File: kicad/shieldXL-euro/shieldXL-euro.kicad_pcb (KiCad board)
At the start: 2 copper layers, 98 x 108 mm, 134 parts, among them J101 Eurorack power, J102 IN L, J103 IN R, J104 OUT L, J105 OUT R, J106 MIDI IN, J107 MIDI OUT, J108 DX07S024WJ1R350, J109 USB 1, J110 USB 2, J111 USB 3, J112 Pi USB, inner stack, J113 Pi USB, outer stack, J115 CORONE I/1, J116 CORONE I/2, J117 CORONE O/1, J118 CORONE O/2, J119 CORONE O/3, J120 CORONE O/4, J121 Corone, J122 ii, Q1 ASFL1-12.288MHZ-LCS-T, SW1 D6R00 F1 LFS, SW2 D6R00 F1 LFS, SW3 D6R00 F1 LFS, U1 CS4270, U101 TL074, U11 TPS793475DBVR, U2 HCPL-0631-500E, X1 RASPI_BOARD_B+#_E3

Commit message: Board: MIDI LEDs on their panel holes, locked
D1 / D2 (red 3 mm) at panel (50.35, 96.5) / (50.35, 102.5) between the MIDI
jacks; F8 had left shieldXL's 0603 LEDs beside them under the same
references, removed. Panel layer redrawn with the LED holes and marks.

Co-Authored-By: Claude Opus 5.5 <noreply@anthropic.com>
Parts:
- added C114: 47u 10V, Capacitor_SMD:C_1206_3216Metric, F.Cu at (85.2, 167.3)
- added C115: 47u 10V, Capacitor_SMD:C_1206_3216Metric, F.Cu at (85.2, 170.6)
- added C116: 47u 10V, Capacitor_SMD:C_1206_3216Metric, F.Cu at (85.2, 174.0)
- added C117: 100n, Capacitor_SMD:C_0805_2012Metric, F.Cu at (80.2, 167.1)
- added C118: 100n, Capacitor_SMD:C_0805_2012Metric, F.Cu at (80.2, 170.1)
- added C119: 100n, Capacitor_SMD:C_0805_2012Metric, F.Cu at (80.2, 173.1)
- added C120: 100n, Capacitor_SMD:C_0805_2012Metric, F.Cu at (80.2, 176.1)
- added C121: 10u, Capacitor_SMD:C_0805_2012Metric, F.Cu at (80.2, 179.1)
- added C122: 100n, Capacitor_SMD:C_0805_2012Metric, F.Cu at (80.2, 182.1)
- added JP103: AGND-GND, Jumper:SolderJumper-2_P1.3mm_Open_Pad1.0x1.5mm, F.Cu at (84.6, 177.4)
- added U102: USBLC6-2SC6, Package_TO_SOT_SMD:SOT-23-6, F.Cu at (75.4, 168.0)
- added U103: USBLC6-2SC6, Package_TO_SOT_SMD:SOT-23-6, F.Cu at (75.4, 172.6)
- added U104: USBLC6-2SC6, Package_TO_SOT_SMD:SOT-23-6, F.Cu at (75.4, 177.2)
- added U105: 74LVC1G125, Package_TO_SOT_SMD:SOT-23-5, F.Cu at (75.4, 181.9)
- D1: value RED -> RED 3mm; footprint ShieldXL:CHIPLED_0603_NOOUTLINE -> MMM:LED_3mm_PadsAC; moved to F.Cu
- D2: value BLUE -> RED 3mm; footprint ShieldXL:CHIPLED_0603_NOOUTLINE -> MMM:LED_3mm_PadsAC; moved to F.Cu
- R101, R103: value 100k -> 69.8k
- R102, R104: value 40.2k -> 30.1k
- R17: value 47Ω -> 100Ω
- R19: value 47Ω -> 470Ω
- R20: value 15Ω -> 470Ω
- moved D2 72.9 mm to (150.3, 132.5)
- moved D1 65.7 mm to (150.3, 126.5)
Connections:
- C105 pad 1: /eurorack/INL_SUM -> /eurorack/INL_DIV
- C105 pad 2: IN_L_LINE -> AGND
- C106 pad 1: /eurorack/INR_SUM -> /eurorack/INR_DIV
- C106 pad 2: IN_R_LINE -> AGND
- D2 pad C: MIDI_TX -> MIDI_TX_BUF
- R101 pad 2: /eurorack/INL_SUM -> /eurorack/INL_DIV
- R102 pad 1: /eurorack/INL_SUM -> /eurorack/INL_DIV
- R102 pad 2: IN_L_LINE -> AGND
- R103 pad 2: /eurorack/INR_SUM -> /eurorack/INR_DIV
- R104 pad 1: /eurorack/INR_SUM -> /eurorack/INR_DIV
- R104 pad 2: IN_R_LINE -> AGND
- R17 pad 2: MIDI_TX -> MIDI_TX_BUF
- U101 pad 2: /eurorack/INL_SUM -> IN_L_LINE
- U101 pad 3: AGND -> /eurorack/INL_DIV
- U101 pad 5: AGND -> /eurorack/INR_DIV
- U101 pad 6: /eurorack/INR_SUM -> IN_R_LINE
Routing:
- net IN_R_LINE: track 15.8 -> 35.9 mm
- net /eurorack/INR_SUM: track 20.0 -> 0.00 mm
- net IN_L_LINE: track 6.16 -> 18.2 mm
- net /eurorack/INL_SUM: track 12.1 -> 0.00 mm

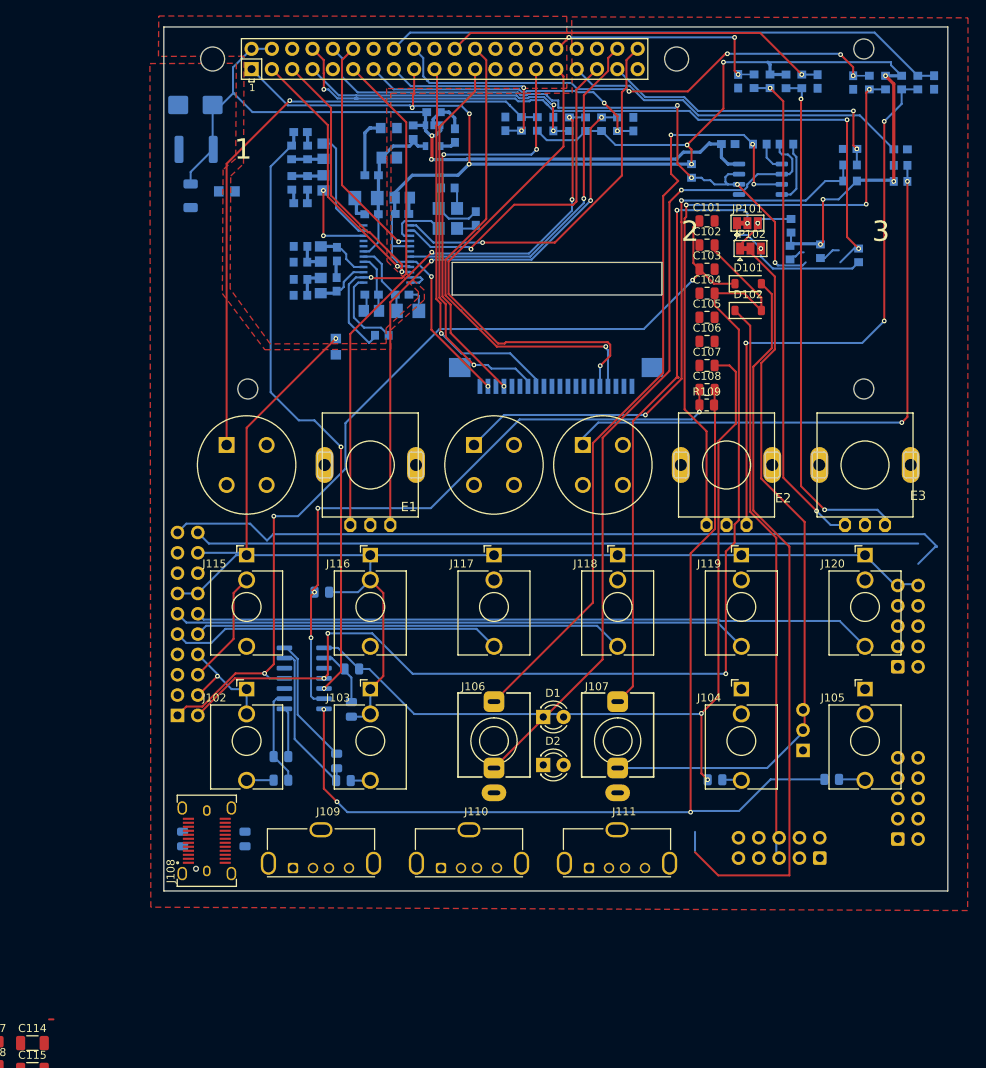
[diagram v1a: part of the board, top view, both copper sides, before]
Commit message: Net classes applied; all tracks and vias removed for the reroute
tools/set_netclasses.py: Power_5V 1.5 mm, USB_VBUS 0.8, Rails_12V 0.5,
Ground 0.5, Logic_Supply 0.4, USB_Data 0.3 (pairs 0.3/0.2), Audio 0.3,
Default 0.25. 771 tracks and 103 vias left over from shieldXL's layout are
gone; the pours are refilled.

Co-Authored-By: Claude Opus 5.5 <noreply@anthropic.com>
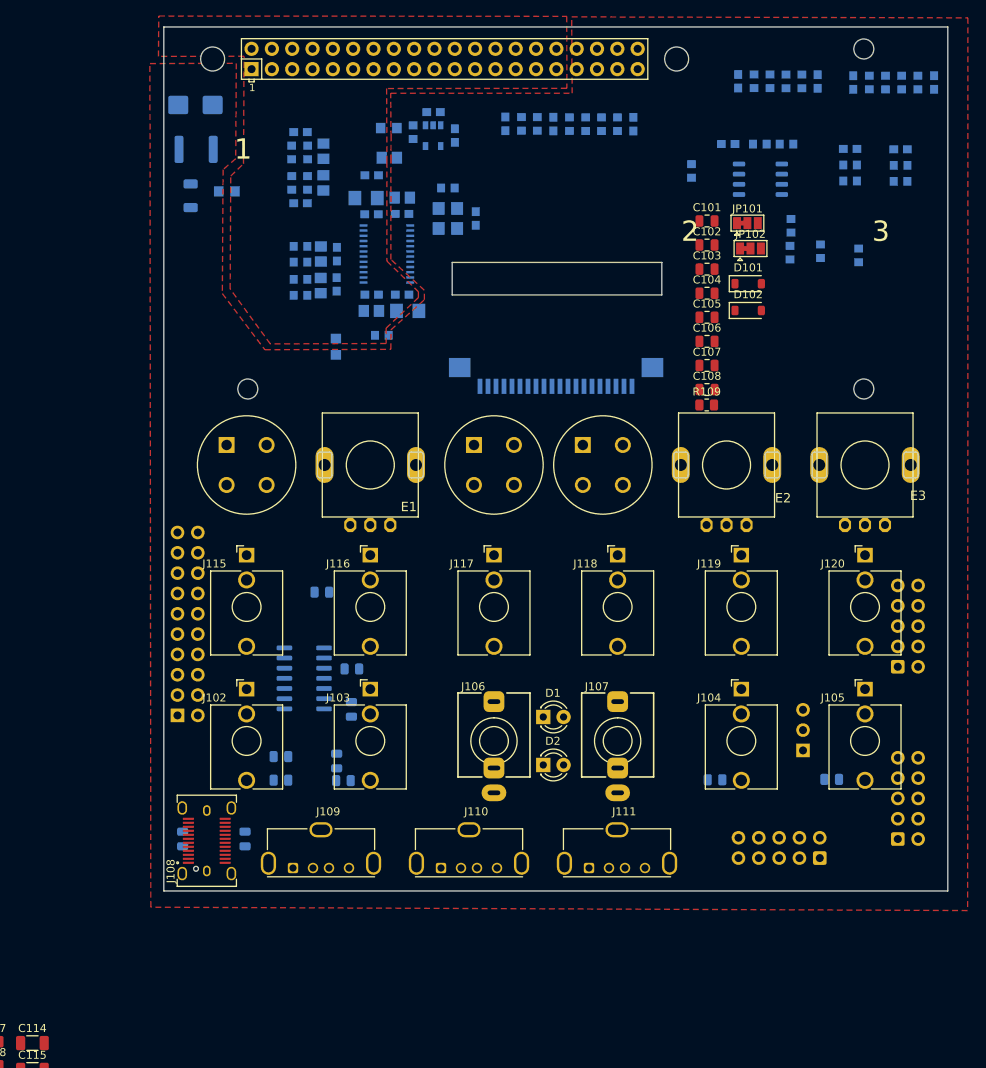
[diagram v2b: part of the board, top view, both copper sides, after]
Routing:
- net +3V3: track 220.6 -> 0.00 mm, vias 12 -> 0
- net AGND: track 197.4 -> 0.00 mm, vias 2 -> 0
- net -12V: track 142.2 -> 0.00 mm, vias 3 -> 0
- net /eurorack/OUTR_AMP: track 129.4 -> 0.00 mm, vias 3 -> 0
- net +12V: track 117.4 -> 0.00 mm, vias 3 -> 0
- net /eurorack/OUTL_AMP: track 106.7 -> 0.00 mm, vias 2 -> 0
- net MIDI_IN_RING: track 101.4 -> 0.00 mm, vias 1 -> 0
- net /eurorack/II_SCL: track 100.5 -> 0.00 mm
- net MIDI_IN_TIP: track 100.0 -> 0.00 mm, vias 3 -> 0
- net +5V: track 98.5 -> 0.00 mm, vias 2 -> 0
- net /eurorack/+12V_IN: track 92.9 -> 0.00 mm
- net MIDI_TX: track 92.5 -> 0.00 mm, vias 3 -> 0
- net /eurorack/II_SDA: track 90.6 -> 0.00 mm
- net /eurorack/MIDI_OUT_R: track 89.3 -> 0.00 mm, vias 1 -> 0
- net /eurorack/CRW_OUT4: track 85.1 -> 0.00 mm
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
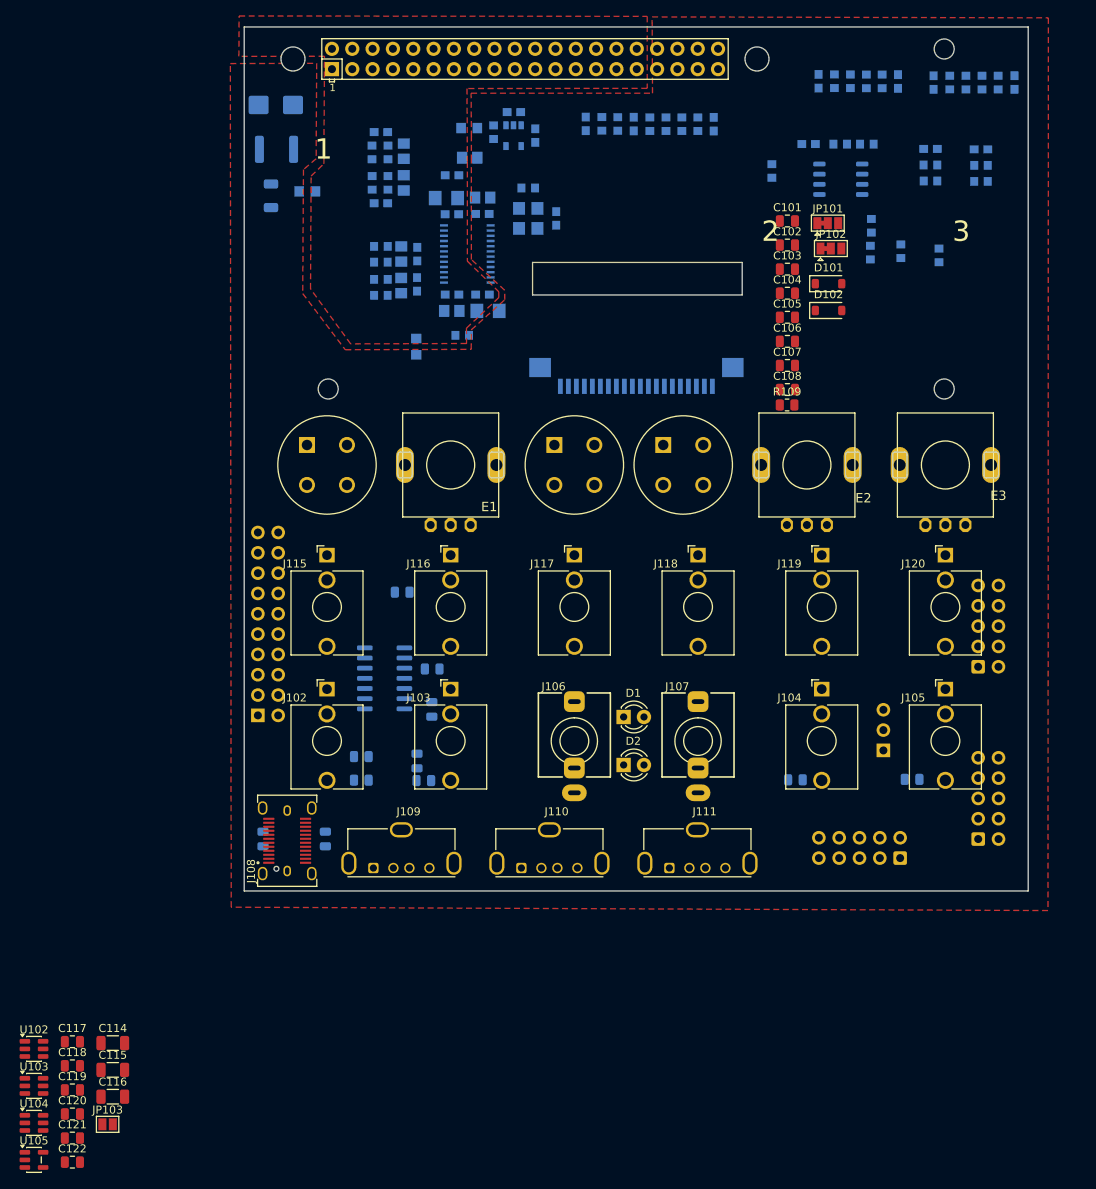
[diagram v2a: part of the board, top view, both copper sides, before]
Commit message: Board: routed (first full route, before ground stitching)
Co-Authored-By: Claude Opus 5.5 <noreply@anthropic.com>
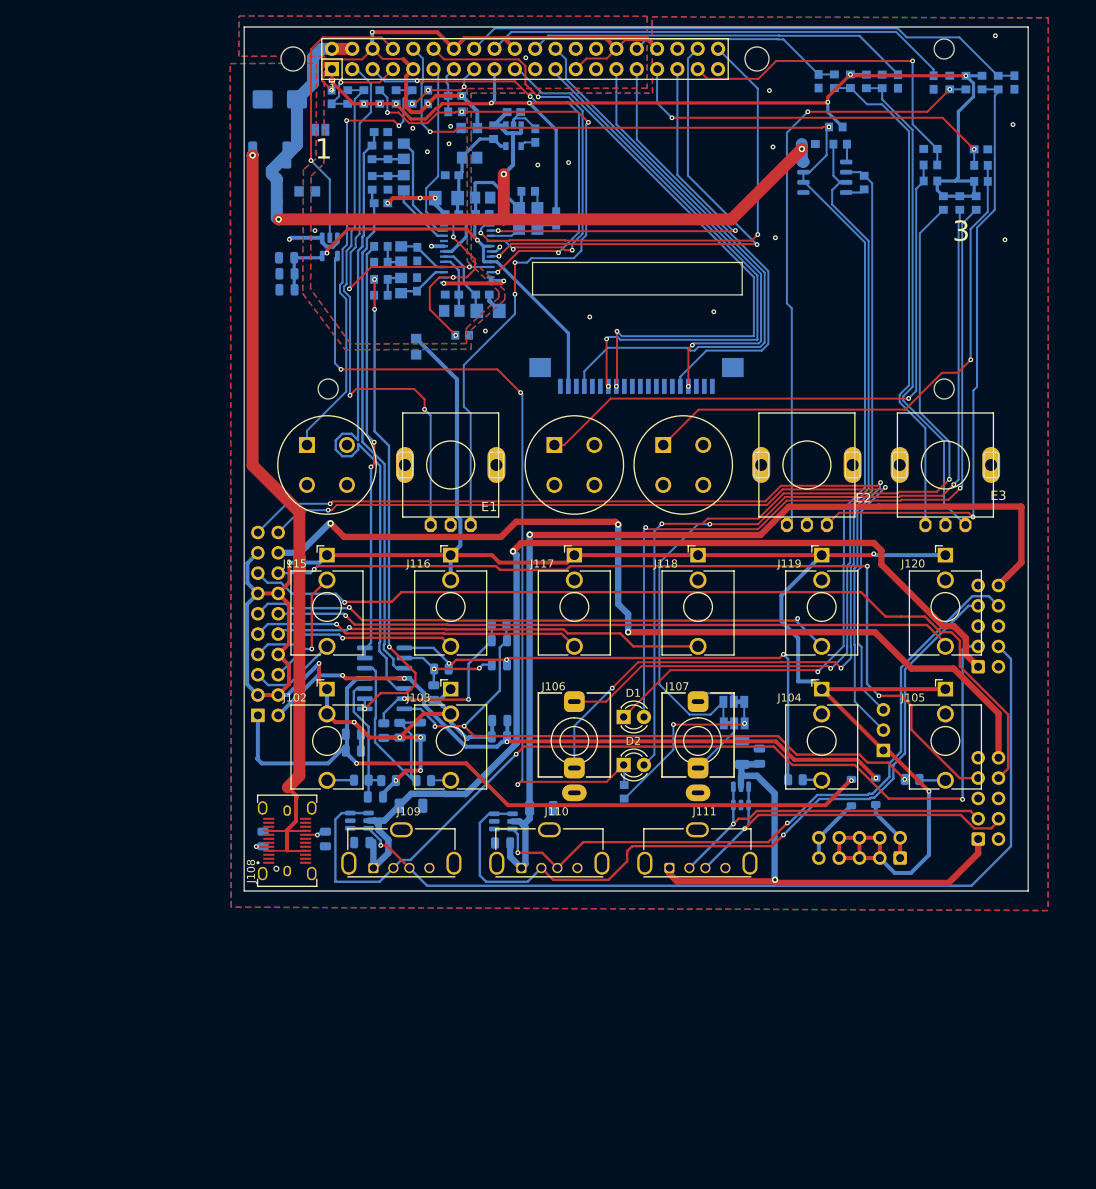
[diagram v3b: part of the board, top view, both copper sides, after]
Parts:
- C101, C102, C103, C104, C105, C106, C107, C108, C114, C115, C116, C117, C118, C119, C120, C121, C122, D101, D102, JP101, JP102, JP103, R109, U102, U103, U104, U105: moved to B.Cu
- moved JP103 127.1 mm to (111.2, 53.1), turned to 180 degrees
- moved U105 120.0 mm to (112.3, 67.7), turned to -90 degrees
- moved C122 116.2 mm to (107.0, 69.1), turned to 180 degrees
- moved C121 111.3 mm to (107.0, 71.1), turned to 180 degrees
- moved C120 106.5 mm to (107.0, 73.1), turned to 180 degrees
- moved U104 97.4 mm to (163.8, 136.4), turned to 90 degrees
- moved C119 95.5 mm to (166.1, 131.4), turned to 90 degrees
- moved C116 89.7 mm to (163.9, 130.9), turned to 90 degrees
- moved C101 85.6 mm to (115.3, 130.8)
- moved C103 79.5 mm to (115.3, 128.7)
- moved C105 79.0 mm to (118.0, 136.5)
- moved R17 77.7 mm to (149.2, 135.8)
- moved C102 69.5 mm to (133.6, 127.0)
- moved U103 67.4 mm to (134.1, 139.6)
- moved C106 66.8 mm to (123.7, 128.2), turned to -90 degrees
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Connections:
- J121 pad 17: /eurorack/CRW_USB_VBUS -> AGND
- J121 pad 18: AGND -> /eurorack/CRW_USB_VBUS
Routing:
- net AGND: track 0.00 -> 328.6 mm, vias 0 -> 19
- net +3V3: track 0.00 -> 214.5 mm, vias 0 -> 10
- net MIDI_RX: track 0.00 -> 163.7 mm, vias 0 -> 3
- net /eurorack/USB1_VBUS: track 0.00 -> 124.6 mm, vias 0 -> 1
- net /eurorack/USB2_VBUS: track 0.00 -> 121.5 mm, vias 0 -> 1
- net /eurorack/USB1_DM: track 0.00 -> 120.8 mm, vias 0 -> 2
- net +5V: track 0.00 -> 119.3 mm, vias 0 -> 3
- net GND: track 0.00 -> 118.8 mm, vias 0 -> 19
- net /eurorack/CRW_USB_VBUS: track 0.00 -> 115.7 mm, vias 0 -> 3
- net /eurorack/II_SCL: track 0.00 -> 114.2 mm, vias 0 -> 2
- net /eurorack/USB1_DP: track 0.00 -> 113.6 mm, vias 0 -> 1
- net /eurorack/CRW_USB_DP: track 0.00 -> 112.5 mm, vias 0 -> 1
- net /eurorack/CRW_USB_DM: track 0.00 -> 109.6 mm, vias 0 -> 3
- net /eurorack/II_SDA: track 0.00 -> 108.8 mm, vias 0 -> 2
- net /eurorack/VBUS_C: track 0.00 -> 108.4 mm, vias 0 -> 1
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- added copper zone on B.Cu, net AGND
- added copper zone on B.Cu, net GND

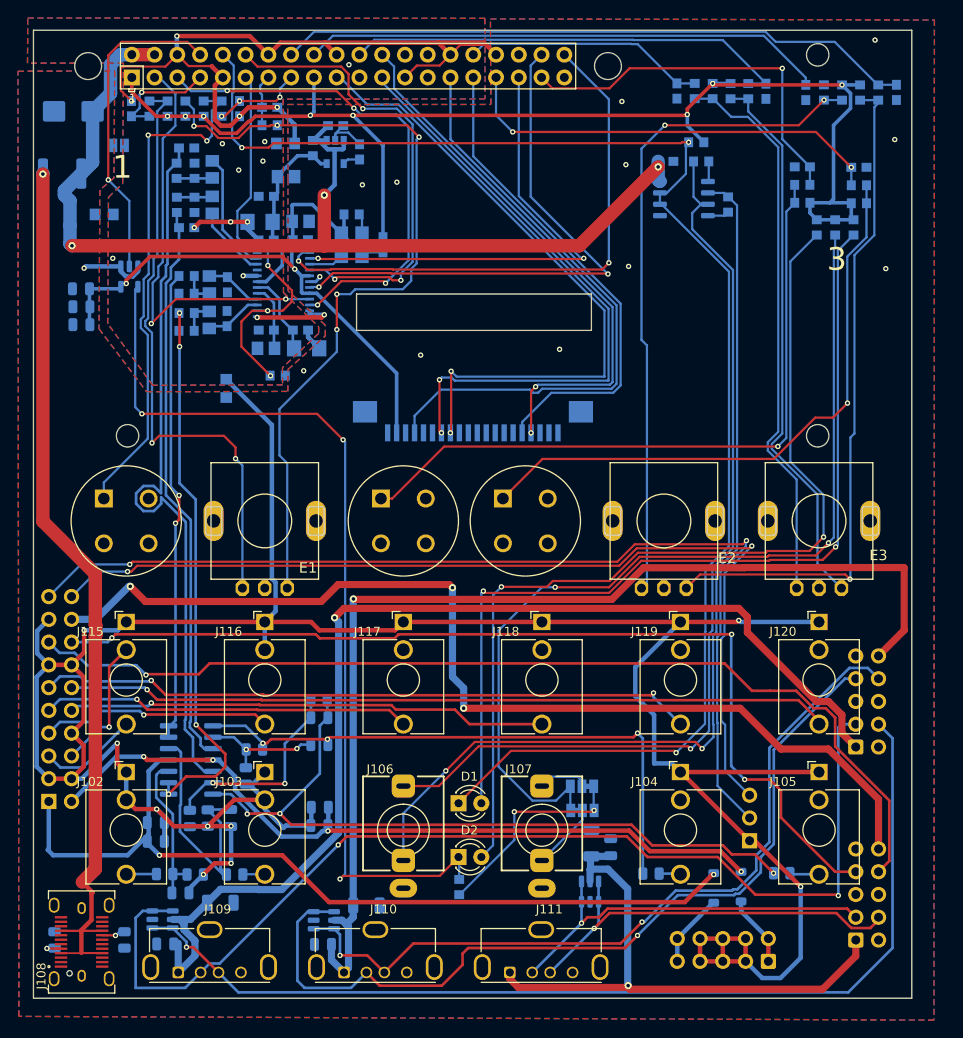
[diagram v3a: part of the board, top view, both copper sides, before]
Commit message: Ground stitching: 81 GND and 5 AGND vias; pours tidied; Power_5V 0.2
tools/stitch_ground.py: AGND's pour now outranks GND's (7 over 6), both drop
unconnected islands, and vias go on a 5 mm grid wherever one fits inside the
same ground's fill on both layers (so clear of every track), then one into
any island still on its own. Unconnected items 9 -> 2; the net classes are
applied, so J108's pads no longer trip Power_5V's clearance.

Co-Authored-By: Claude Opus 5.5 <noreply@anthropic.com>
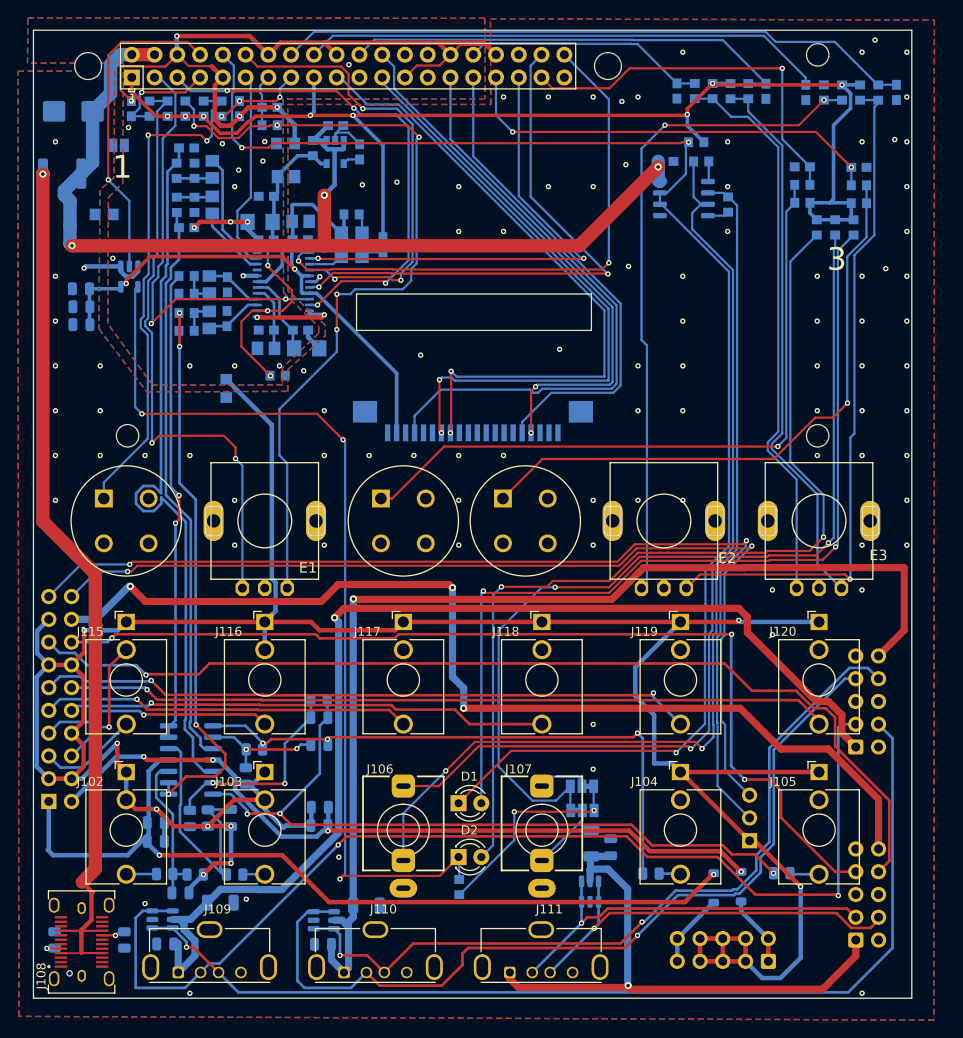
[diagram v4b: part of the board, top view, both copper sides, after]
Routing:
- net GND: vias 19 -> 100
- net AGND: vias 19 -> 24

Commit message: Board: routed, DRC connectivity clean (0 unconnected, parity clean)
Co-Authored-By: Claude Opus 5.5 <noreply@anthropic.com>
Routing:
- net AGND: track 328.6 -> 340.5 mm
- net OUT_R_LINE: track 81.4 -> 73.0 mm
- net GND: track 118.8 -> 126.8 mm, vias 100 -> 102
- net /norns-shield-210330_1/SDA: track 48.3 -> 42.1 mm
- removed copper zone on B.Cu, net +3V3
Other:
- board text removed: "20230615"
- board text removed: "JLCJLCJLCJLC"
- board text removed: "MIDI IN"
- board text removed: "MIDI OUT"
- board text removed: "SHIELDXL DESKTOP BOARD - PARTS STASH"
- board text removed: "\\\\\\\\\\"
- board text removed: "based on the 210330 norns shield designed by monome remixed march 2023 by denki-oto. no official support - do not ask monome for help https://github.com/okyeron/shieldXL open source hardware GPLv3"
- board text removed: "shieldXL"
